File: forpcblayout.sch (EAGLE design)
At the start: 73 parts, among them J1 3x2 M, J2 S2B-PH-SM4-TB(LF)(SN), J3 629105136821, SW1 AYZ0202AGRLC, SW2 !RESET, T1 2N2222, T2 2N2222, T3 2N2222, T4 2N2222, U1 MCP73831, U2 MIC5219, U3 ATMEGA32U4-AUR, X2 16 MHz

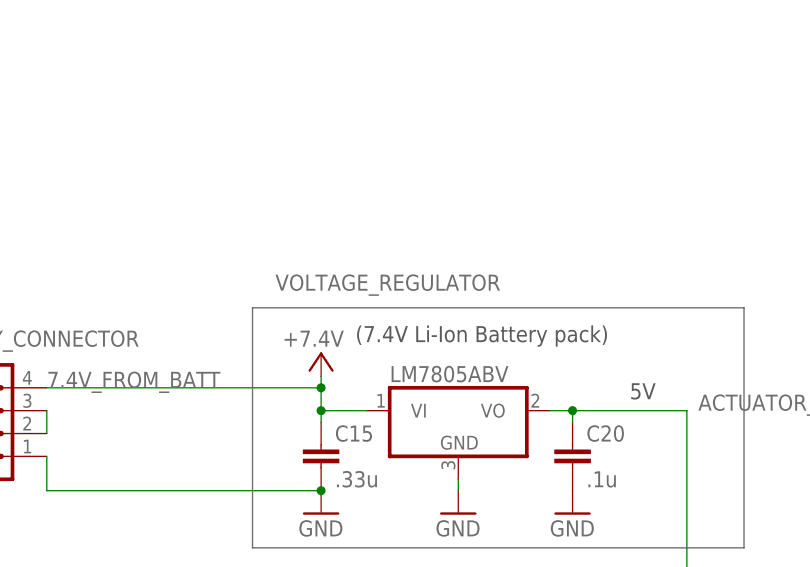
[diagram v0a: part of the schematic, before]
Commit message: Added H-Bridge to Board
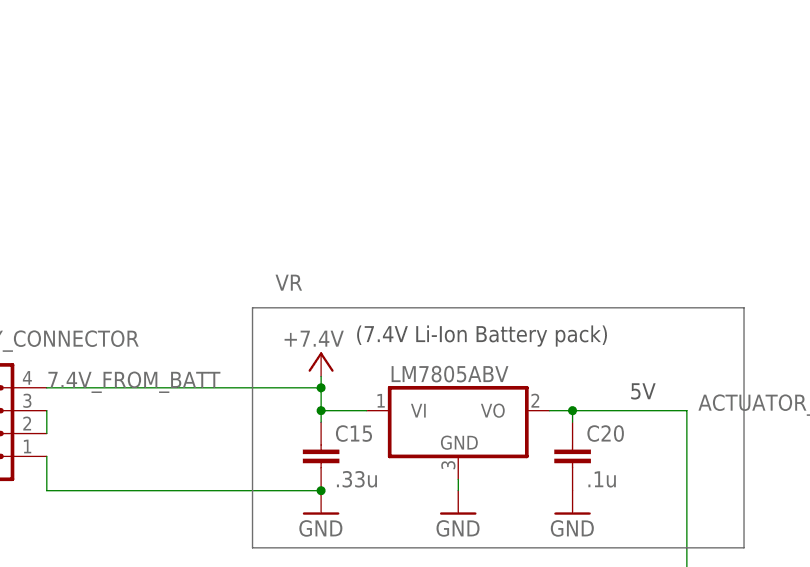
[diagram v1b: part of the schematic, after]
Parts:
- renumbered VOLTAGE_REGULATOR to VR
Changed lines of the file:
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@@
 <?xml version="1.0" encoding="utf-8"?>
 <!DOCTYPE eagle SYSTEM "eagle.dtd">
-<eagle version="9.3.2">
+<eagle version="9.5.2">
 <drawing>
 <settings>
@@
 <part name="SUPPLY2" library="SparkFun-PowerSymbols" library_urn="urn:adsk.eagle:library:530" deviceset="V_BATT" device=""/>
 <part name="P+4" library="supply1" library_urn="urn:adsk.eagle:library:371" deviceset="+5V" device="" value="+7.4V"/>
-<part name="VOLTAGE_REGULATOR" library="linear" library_urn="urn:adsk.eagle:library:262" deviceset="78*" device="H" package3d_urn="urn:adsk.eagle:package:16419/1" technology="05" value="LM7805ABV">
+<part name="VR" library="linear" library_urn="urn:adsk.eagle:library:262" deviceset="78*" device="H" package3d_urn="urn:adsk.eagle:package:16419/1" technology="05" value="LM7805ABV">
 <attribute name="SPICEPREFIX" value="J"/>
 </part>
@@
 <attribute name="VALUE" x="342.9" y="129.54" size="1.778" layer="96" rot="R180"/>
 </instance>
-<instance part="VOLTAGE_REGULATOR" gate="A1" x="355.6" y="120.65" smashed="yes">
+<instance part="VR" gate="A1" x="355.6" y="120.65" smashed="yes">
 <attribute name="NAME" x="335.28" y="133.985" size="1.778" layer="95"/>
 <attribute name="VALUE" x="347.98" y="123.825" size="1.778" layer="96"/>
@@
 </segment>
 <segment>
-<pinref part="VOLTAGE_REGULATOR" gate="A1" pin="GND"/>
+<pinref part="VR" gate="A1" pin="GND"/>
 <wire x1="355.6" y1="113.03" x2="355.6" y2="111.76" width="0.1524" layer="91"/>
 <pinref part="GND22" gate="1" pin="GND"/>
@@
 <wire x1="309.88" y1="123.19" x2="340.36" y2="123.19" width="0.1524" layer="91"/>
 <junction x="340.36" y="123.19"/>
-<pinref part="VOLTAGE_REGULATOR" gate="A1" pin="VI"/>
+<pinref part="VR" gate="A1" pin="VI"/>
 <wire x1="345.44" y1="120.65" x2="340.36" y2="120.65" width="0.1524" layer="91"/>
 <junction x="340.36" y="120.65"/>
@@
 <pinref part="C20" gate="G$1" pin="1"/>
 <wire x1="368.3" y1="119.38" x2="368.3" y2="120.65" width="0.1524" layer="91"/>
-<pinref part="VOLTAGE_REGULATOR" gate="A1" pin="VO"/>
+<pinref part="VR" gate="A1" pin="VO"/>
 <wire x1="365.76" y1="120.65" x2="368.3" y2="120.65" width="0.1524" layer="91"/>
 <wire x1="368.3" y1="120.65" x2="381" y2="120.65" width="0.1524" layer="91"/>

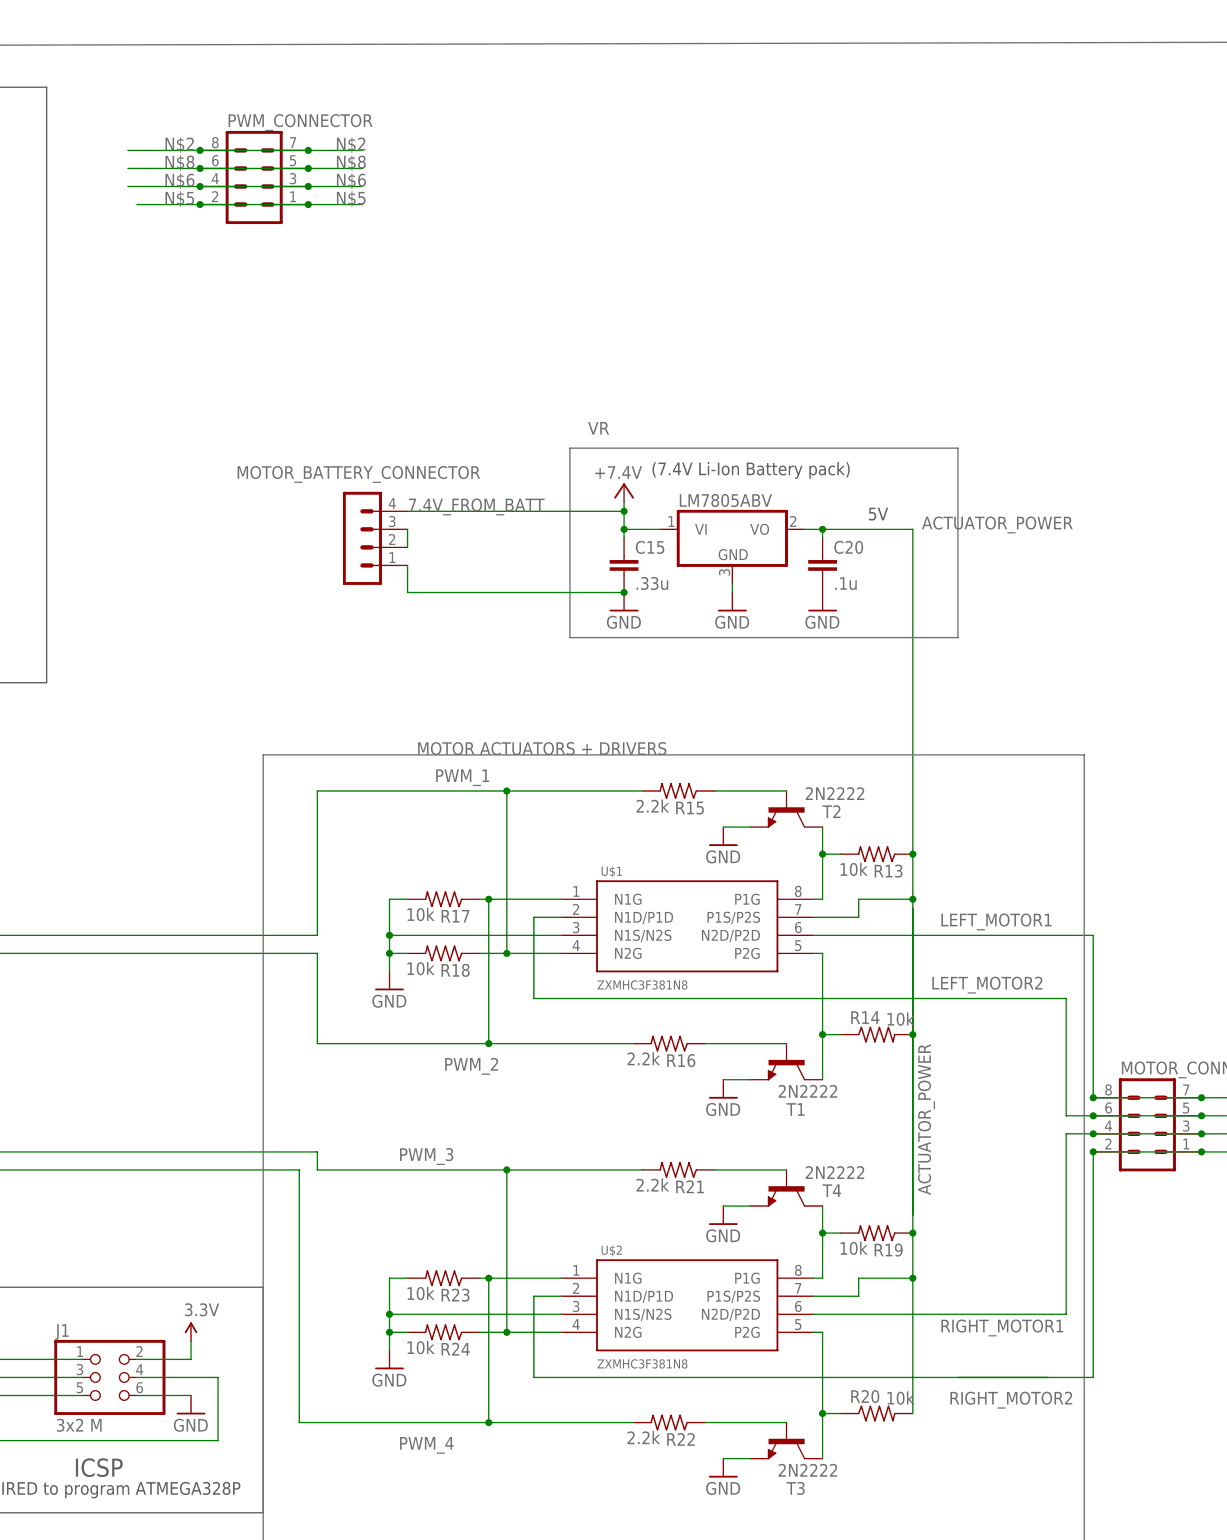
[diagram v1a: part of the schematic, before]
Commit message: Fixed routing mistakes, extended board edge to clear matrix
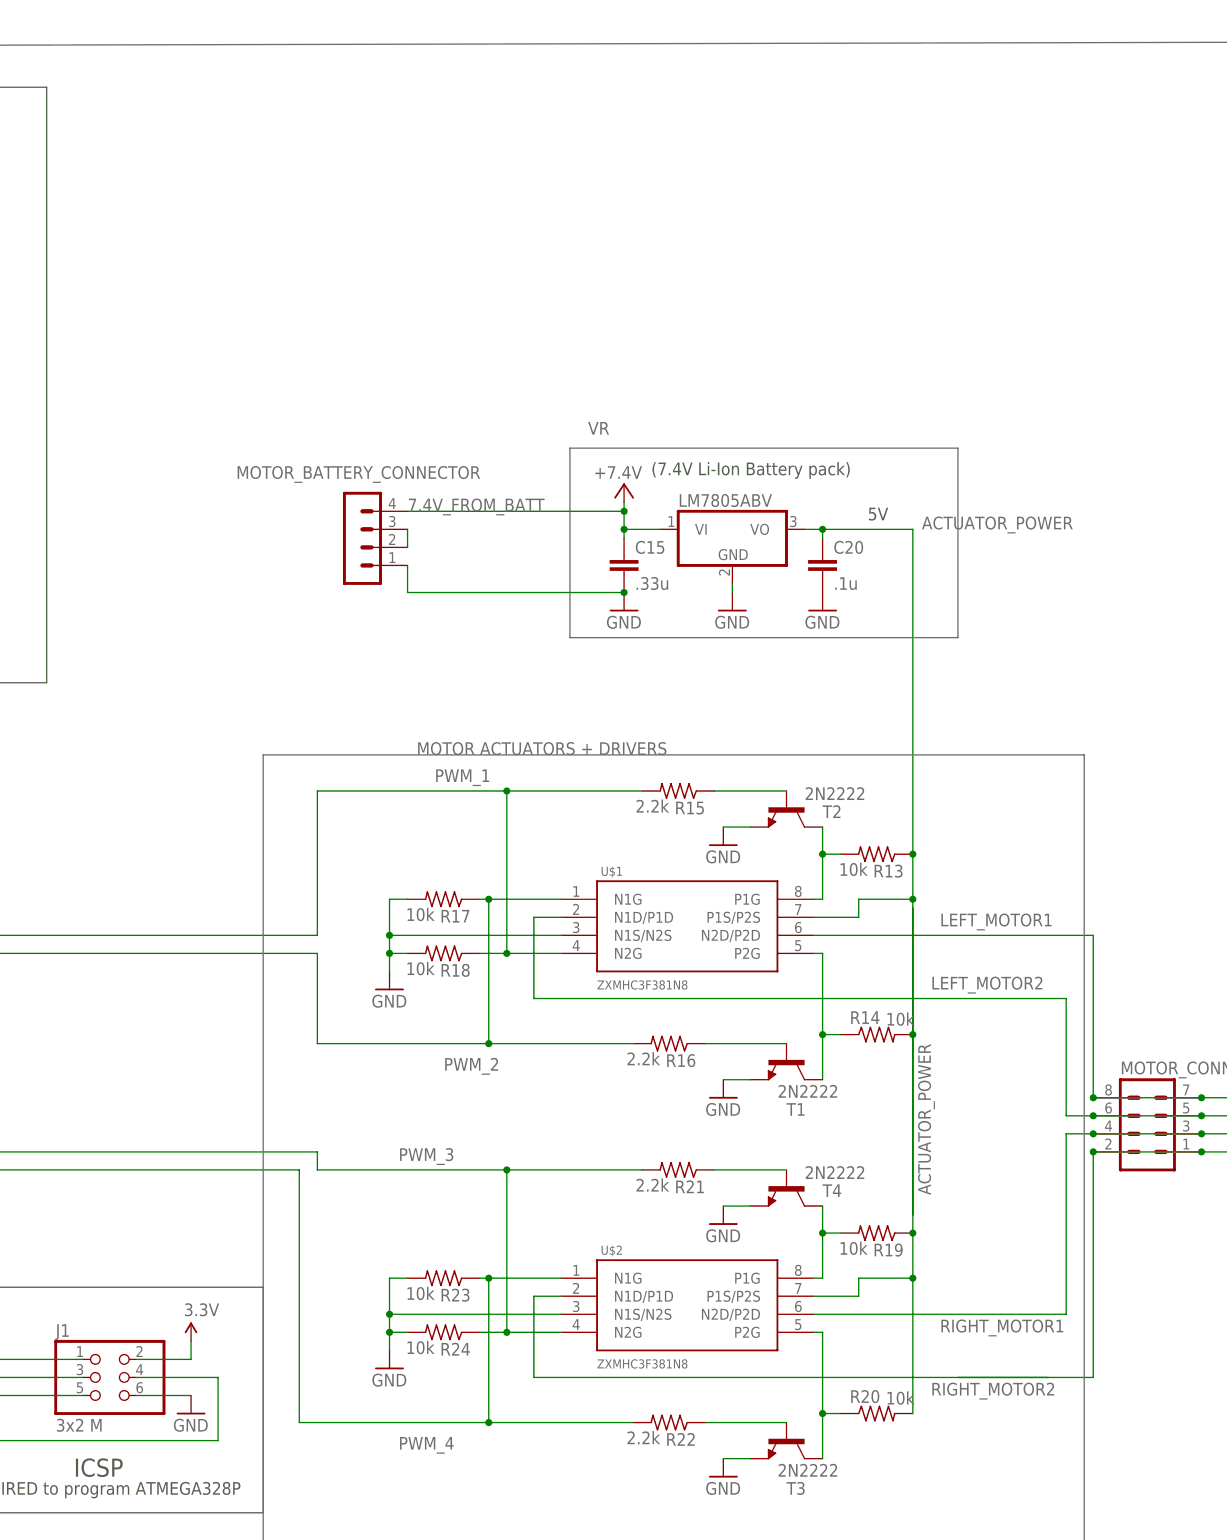
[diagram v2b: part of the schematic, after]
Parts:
- removed PWM_CONNECTOR: (no value), con-lstb:MA04-2
- VR: device linear:7805H -> linear:7805T
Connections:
- removed net N$2: PWM_CONNECTOR.7, PWM_CONNECTOR.8
- removed net N$5: PWM_CONNECTOR.1, PWM_CONNECTOR.2
- removed net N$6: PWM_CONNECTOR.3, PWM_CONNECTOR.4
- removed net N$8: PWM_CONNECTOR.5, PWM_CONNECTOR.6
- net LEFT_MOTOR2: no longer U$2.N1D/P1D
- net RIGHT_MOTOR2: now also U$2.N1D/P1D

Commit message: Added in 0ohm resistors and added in vias (for stitching)
GND Plane is still a question mark, vias don't seem to be part of flooded planes. Also DRC claims GND pins aren't connected to GND plane
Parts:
- added R25, R26, R27, R28, R29, R30, R31, R32, R33, R34, R35, R36, R37, R38, R39, R40, R41: 0, rcl:R-US_R0805
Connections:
- removed net (5V@2.1A): R7.2, R9.2
- removed net H_BRIDGE_POWER: C20.1, R13.1, R14.2, U$1.P1S/P2S, VR.VO
- removed net H_BRIDGE_POWER1: R19.1, R20.2, U$2.P1S/P2S
- new net 7.4_FROM_BATT: C15.1, R37.1, VR.VI
- new net ACTUATOR_POWER: C20.1, R19.1, R20.2, R31.2, U$2.P1S/P2S, VR.VO
- new net ACUATOR_POWER: R13.1, R14.2, R31.1, U$1.P1S/P2S
- new net N$159: J3.VBUS, R39.2
- new net VBAT: R40.2, U1.VBAT
- net !RESET: now also R38.1, R38.2
- net 3.3V: now also R41.1, R41.2
- net 7.4V_FROM_BATT: now also R37.2; no longer C15.1, VR.VI
- net LEFT_MOTOR1: now also R36.1, R36.2
- net LEFT_MOTOR2: now also R35.1, R35.2
- net POWER_IN: now also R32.1, R32.2, R7.2, R9.2
- net PWM_1: now also R28.1, R28.2
- net PWM_2: now also R27.1, R27.2
- net PWM_3: now also R25.1, R25.2
- net PWM_4: now also R26.1, R26.2
- net RIGHT_MOTOR1: now also R33.1, R33.2
- net RIGHT_MOTOR2: now also R34.1, R34.2
- net SCLK: now also R29.1, R29.2
- net SDA: now also R30.1, R30.2
- net VBUS: now also R39.1; no longer J3.VBUS
- net V_BATT: now also R40.1; no longer U1.VBAT
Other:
- note removed: "The two motors shown are for the left and right tires of the chassis Using half H-bridges (only want to turn in forward direction) and PWM we're hoping that we'll be able to control said motors."
- moved on the sheet: C8, C9

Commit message: Changed 0ohm resistors to through hole
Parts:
- R25, R26, R27, R28, R29, R30, R31, R32, R33, R34, R35, R36, R37, R38, R39, R40, R41: device rcl:R-US_R0805 -> rcl:R-US_0207/2V
- renumbered U$1 to LEFT_H_BRIDGE, U$2 to RIGHT_H_BRIDGE
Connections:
- removed net N$159: J3.VBUS, R39.2
- net VBUS: now also J3.VBUS, R39.2
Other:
- note added: "(+)"
- note added: "(-)"
- note added: "4 PWM signals come in from the Atmega processor to 2 H bridges. Each H bridge then controls a motor, being able to turn in forward or backward as needed."
- note added: "5V Voltage Regulator"
- note added: "A 2x20 GPIO header be attached with female connections available on the bottom layer (connects to Pi) and male connections on the top layer (connects to Matrix). The Atmega will share the I2C line with the Pi & Matrix as well as get its Power and GND from the Pi's Li-Ion power pack."
- note added: "Arduino Lilypad Rev 10 schemtatic used was taken from this repo: https://github.com/andrewgreenberg/eaglecad-things"
- note added: "FROM PI'S POWER PACK"
- note added: "RASP_PI GPIO PIN HEADER EXTENDED"
- note removed: "(7.4V Li-Ion Battery pack)"
- note removed: "ATMEGA PROCESSOR IN LILYPAD SCHEMATIC"
- note removed: "Originally taken from AndrewGreenburg/Eaglecad-things repo"
- moved on the sheet: MOTOR_BATTERY_CONNECTOR, R37, SV1

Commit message: Changed just about everything
Jk, changed wire widths, stitched properly, passed ERC as well as DRC
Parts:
- removed C1: 470p, rcl:C-EUC0805K
- removed C6, C8: 4.7u, rcl:C-EUC0805K
- removed C9: 100n, rcl:C-EUC0805K
- removed D5: GREEN, led:LEDCHIP-LED0805
- removed J2: S2B-PH-SM4-TB(LF)(SN), SparkFun-Connectors:M02-JST-2MM-SMT
- removed R1: 1K, rcl:R-US_R0805
- removed R2: 10K, rcl:R-US_R0805
- removed R40, R41: 0, rcl:R-US_0207/2V
- removed SW1: AYZ0202AGRLC, SparkFun-Electromechanical:SWITCH-DPDTSMD
- removed U1: MCP73831, SparkFun-PowerIC:MCP73831
- removed U2: MIC5219, SparkFun-PowerIC:V_REG_MIC5219SMD
- MOTOR_BATTERY_CONNECTOR: value (none) -> MOTOR_BATTERY_CONNECTOR
- MOTOR_CONNECTOR: value (none) -> MOTOR_CONNECTOR
- R7, R9: value 1K -> 4.7K
- SV1: value (none) -> EXTENDED PIN HEADER
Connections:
- net 7.4_FROM_BATT renamed 7.4_FROM_BATT_0
- removed net 3.3V: C8.1, C9.1, J1.2, R10.2, R12.2, R3.2, R41.1, R41.2, R8.2, U2.OUT
- removed net ACUATOR_POWER: LEFT_H_BRIDGE.P1S/P2S, R13.1, R14.2, R31.1
- removed net MCPPROG: R2.2, U1.PROG
- removed net MIC-BP: C1.1, U2.BP
- removed net MIC-EN: SW1.2, U2.EN
- removed net N$3: D5.A, R1.1
- removed net N$4: D5.C, U1.STAT
- removed net PWRIN: C7.1, D1.C, D4.C, SW1.1, U2.IN
- removed net VBAT: R40.2, U1.VBAT
- removed net V_BATT: C6.1, D1.A, J2.1, R40.1
- new net !RESET_0: J1.5, R38.1, TP3.TP
- new net 5V: C11.1, C7.1, D1.C, D4.C, J1.2, R10.2, R12.2, R3.2, R32.2, R7.2, R8.2, R9.2
- new net 5V_0: C10.1, C2.1, C3.1, R32.1, U3.AVCC@24, U3.AVCC@44, U3.VCC@14, U3.VCC@34
- new net ACTUATOR_POWER_0: LEFT_H_BRIDGE.P1S/P2S, R13.1, R14.2, R19.1, R20.2, R31.1, RIGHT_H_BRIDGE.P1S/P2S
- new net LEFT_MOTOR1_0: MOTOR_CONNECTOR.7, MOTOR_CONNECTOR.8, R36.1
- new net LEFT_MOTOR2_0: MOTOR_CONNECTOR.5, MOTOR_CONNECTOR.6, R35.1
- new net PWM_1_0: LEFT_H_BRIDGE.N2G, R15.2, R18.1, R28.1
- new net PWM_2_0: LEFT_H_BRIDGE.N1G, R16.2, R17.1, R27.1
- new net PWM_3_0: R21.2, R24.1, R25.1, RIGHT_H_BRIDGE.N2G
- new net PWM_4_0: R22.2, R23.1, R26.1, RIGHT_H_BRIDGE.N1G
- new net RIGHT_MOTOR1_0: MOTOR_CONNECTOR.1, MOTOR_CONNECTOR.2, R33.2
- new net RIGHT_MOTOR2_0: MOTOR_CONNECTOR.3, MOTOR_CONNECTOR.4, R34.2
- new net SCLK_0: R29.1, U3.PD0(SCL)
- new net SDA_0: R30.1, U3.PD1(SDA)
- new net VBUS_0: C19.1, D4.A, R39.1
- net !RESET: no longer J1.5, R38.1, TP3.TP
- net ACTUATOR_POWER: no longer R19.1, R20.2, RIGHT_H_BRIDGE.P1S/P2S
- net GND: no longer C1.2, C6.2, C8.2, C9.2, J2.2, R2.1, SW1.3, U1.VSS, U2.GND
- net LEFT_MOTOR1: no longer MOTOR_CONNECTOR.7, MOTOR_CONNECTOR.8, R36.1
- net LEFT_MOTOR2: no longer MOTOR_CONNECTOR.5, MOTOR_CONNECTOR.6, R35.1
- net POWER_IN: now also D1.A; no longer C10.1, C11.1, C2.1, C3.1, R32.1, R32.2, R7.2, R9.2, U3.AVCC@24, U3.AVCC@44, U3.VCC@14, U3.VCC@34
- net PWM_1: no longer LEFT_H_BRIDGE.N2G, R15.2, R18.1, R28.1
- net PWM_2: no longer LEFT_H_BRIDGE.N1G, R16.2, R17.1, R27.1
- net PWM_3: no longer R21.2, R24.1, R25.1, RIGHT_H_BRIDGE.N2G
- net PWM_4: no longer R22.2, R23.1, R26.1, RIGHT_H_BRIDGE.N1G
- net RIGHT_MOTOR1: no longer MOTOR_CONNECTOR.3, MOTOR_CONNECTOR.4, R33.2
- net RIGHT_MOTOR2: no longer MOTOR_CONNECTOR.1, MOTOR_CONNECTOR.2, R34.2
- net SCLK: no longer R29.1, U3.PD0(SCL)
- net SDA: no longer R30.1, U3.PD1(SDA)
- net VBUS: no longer C19.1, D4.A, R1.2, R39.1, U1.VIN
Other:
- note removed: "CHARGE"
- moved on the sheet: C10, C11, C15, C16, C17, C18, C19, C2, C20, C3, C4, C5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

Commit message: Traces orthogonal to pads, schematic title, frame value, motor pin de-fucking.
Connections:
- net RIGHT_MOTOR1_0: now also MOTOR_CONNECTOR.3, MOTOR_CONNECTOR.4; no longer MOTOR_CONNECTOR.1, MOTOR_CONNECTOR.2
- net RIGHT_MOTOR2_0: now also MOTOR_CONNECTOR.1, MOTOR_CONNECTOR.2; no longer MOTOR_CONNECTOR.3, MOTOR_CONNECTOR.4
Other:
- note added: "FearBot Controller"
- note added: "Team 13 Bliss Brass Colton Bruce Mike Hall Grace Semerjian"
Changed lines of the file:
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@@
 <?xml version="1.0" encoding="utf-8"?>
 <!DOCTYPE eagle SYSTEM "eagle.dtd">
-<eagle version="9.5.1">
+<eagle version="9.3.2">
 <drawing>
 <settings>
@@
 <part name="SUPPLY6" library="SparkFun-PowerSymbols" library_urn="urn:adsk.eagle:library:530" deviceset="5V" device=""/>
 <part name="SUPPLY7" library="SparkFun-PowerSymbols" library_urn="urn:adsk.eagle:library:530" deviceset="5V" device=""/>
-<part name="FRAME1" library="frames" library_urn="urn:adsk.eagle:library:229" deviceset="FRAME_C_L" device=""/>
+<part name="FRAME1" library="frames" library_urn="urn:adsk.eagle:library:229" deviceset="FRAME_C_L" device="" value="FearBot Controller"/>
 <part name="SUPPLY8" library="SparkFun-PowerSymbols" library_urn="urn:adsk.eagle:library:530" deviceset="5V" device="" value="VBUS_0"/>
 </parts>
@@
 Each H bridge then controls a motor, being able to turn in forward
 or backward as needed. </text>
+<text x="83.82" y="402.59" size="12.7" layer="97">FearBot Controller</text>
+<text x="85.09" y="374.65" size="2.54" layer="97">Team 13
+Bliss Brass
+Colton Bruce
+Mike Hall
+Grace Semerjian</text>
 </plain>
 <instances>
@@
 <segment>
 <pinref part="R33" gate="G$1" pin="2"/>
-<pinref part="MOTOR_CONNECTOR" gate="G$1" pin="2"/>
-<wire x1="508" y1="187.96" x2="508" y2="182.88" width="0.1524" layer="91"/>
-<wire x1="511.81" y1="187.96" x2="508" y2="187.96" width="0.1524" layer="91"/>
+<pinref part="MOTOR_CONNECTOR" gate="G$1" pin="4"/>
+<wire x1="508" y1="190.5" x2="508" y2="182.88" width="0.1524" layer="91"/>
+<wire x1="511.81" y1="190.5" x2="508" y2="190.5" width="0.1524" layer="91"/>
 <label x="528.32" y="187.96" size="1.778" layer="95"/>
-<pinref part="MOTOR_CONNECTOR" gate="G$1" pin="1"/>
-<wire x1="511.81" y1="187.96" x2="527.05" y2="187.96" width="0.1524" layer="91"/>
-<junction x="511.81" y="187.96"/>
+<pinref part="MOTOR_CONNECTOR" gate="G$1" pin="3"/>
+<wire x1="511.81" y1="190.5" x2="527.05" y2="190.5" width="0.1524" layer="91"/>
+<junction x="511.81" y="190.5"/>
 </segment>
 </net>
@@
 <net name="RIGHT_MOTOR2_0" class="0">
 <segment>
-<pinref part="MOTOR_CONNECTOR" gate="G$1" pin="4"/>
+<pinref part="MOTOR_CONNECTOR" gate="G$1" pin="2"/>
 <label x="528.32" y="190.5" size="1.778" layer="95"/>
-<pinref part="MOTOR_CONNECTOR" gate="G$1" pin="3"/>
-<wire x1="511.81" y1="190.5" x2="527.05" y2="190.5" width="0.1524" layer="91"/>
-<junction x="510.54" y="190.5"/>
+<pinref part="MOTOR_CONNECTOR" gate="G$1" pin="1"/>
+<wire x1="511.81" y1="187.96" x2="527.05" y2="187.96" width="0.1524" layer="91"/>
 <pinref part="R34" gate="G$1" pin="2"/>
-<wire x1="511.81" y1="168.91" x2="511.81" y2="186.69" width="0.1524" layer="91"/>
-<wire x1="511.81" y1="186.69" x2="510.54" y2="186.69" width="0.1524" layer="91"/>
-<wire x1="510.54" y1="186.69" x2="510.54" y2="190.5" width="0.1524" layer="91"/>
-<wire x1="510.54" y1="190.5" x2="511.81" y2="190.5" width="0.1524" layer="91"/>
-<junction x="511.81" y="190.5"/>
-</segment>
-</net>
+<wire x1="511.81" y1="168.91" x2="511.81" y2="187.96" width="0.1524" layer="91"/>
+</segment>
+</net>
